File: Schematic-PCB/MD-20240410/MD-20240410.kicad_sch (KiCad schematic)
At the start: 52 parts, among them J1 Conn_01x05_Pin, J2 Conn_01x04_Pin, J3 Conn_01x02_Pin, J4 Conn_01x02_Pin, J5 Conn_01x02_Pin, J6 Conn_01x02_Pin, J7 Conn_01x02_Pin, J8 Conn_01x15_Pin, Q2 PMOS, Q3 NMOS, Q4 NMOS

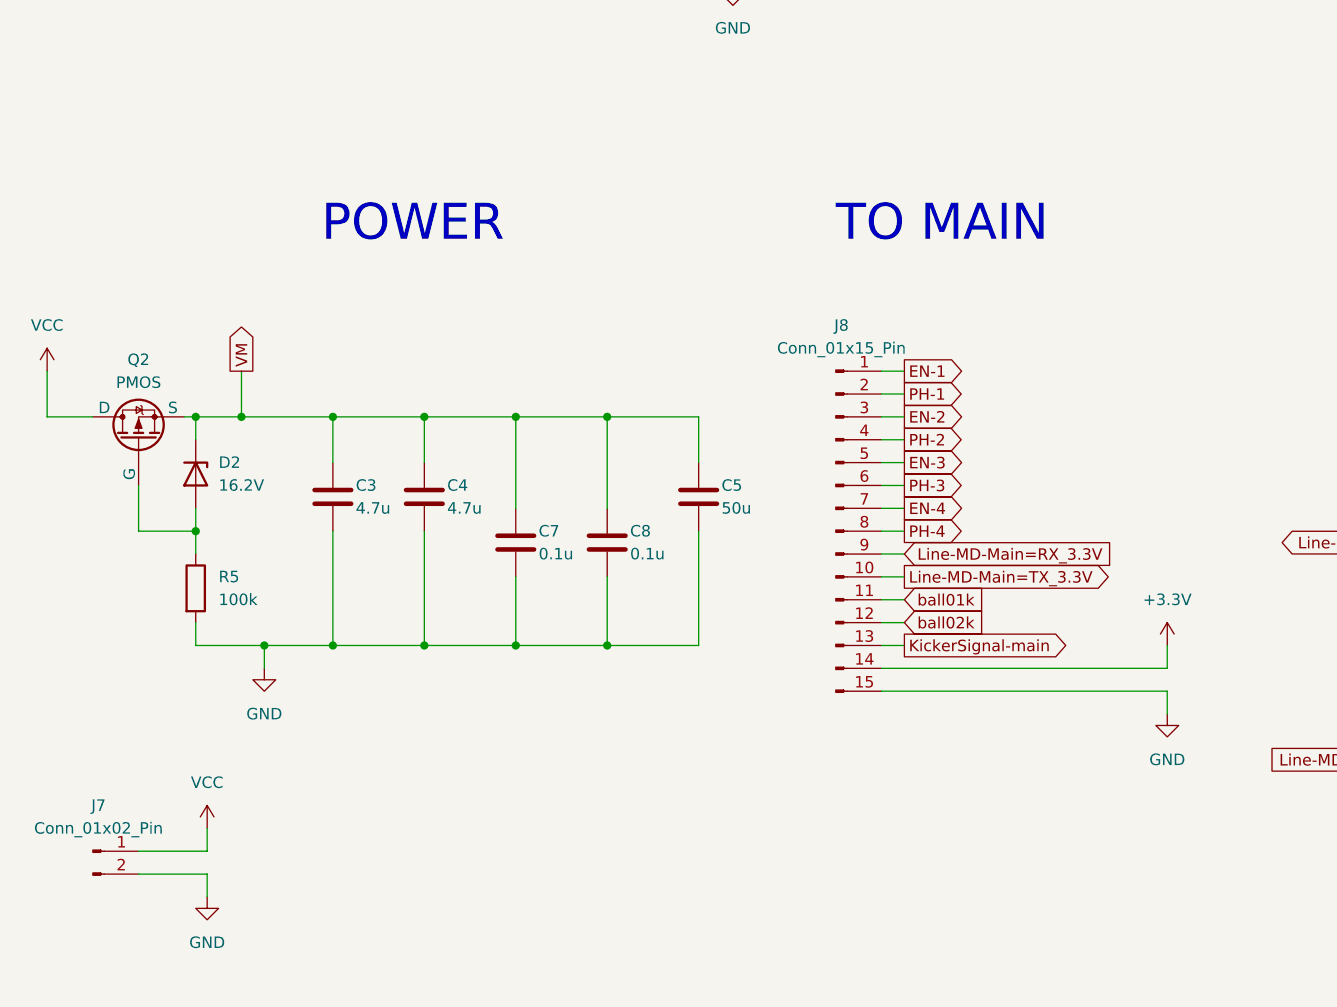
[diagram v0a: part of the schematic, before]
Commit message: MD基板のPCBを更新
回路図のDRを再度お願いしたい
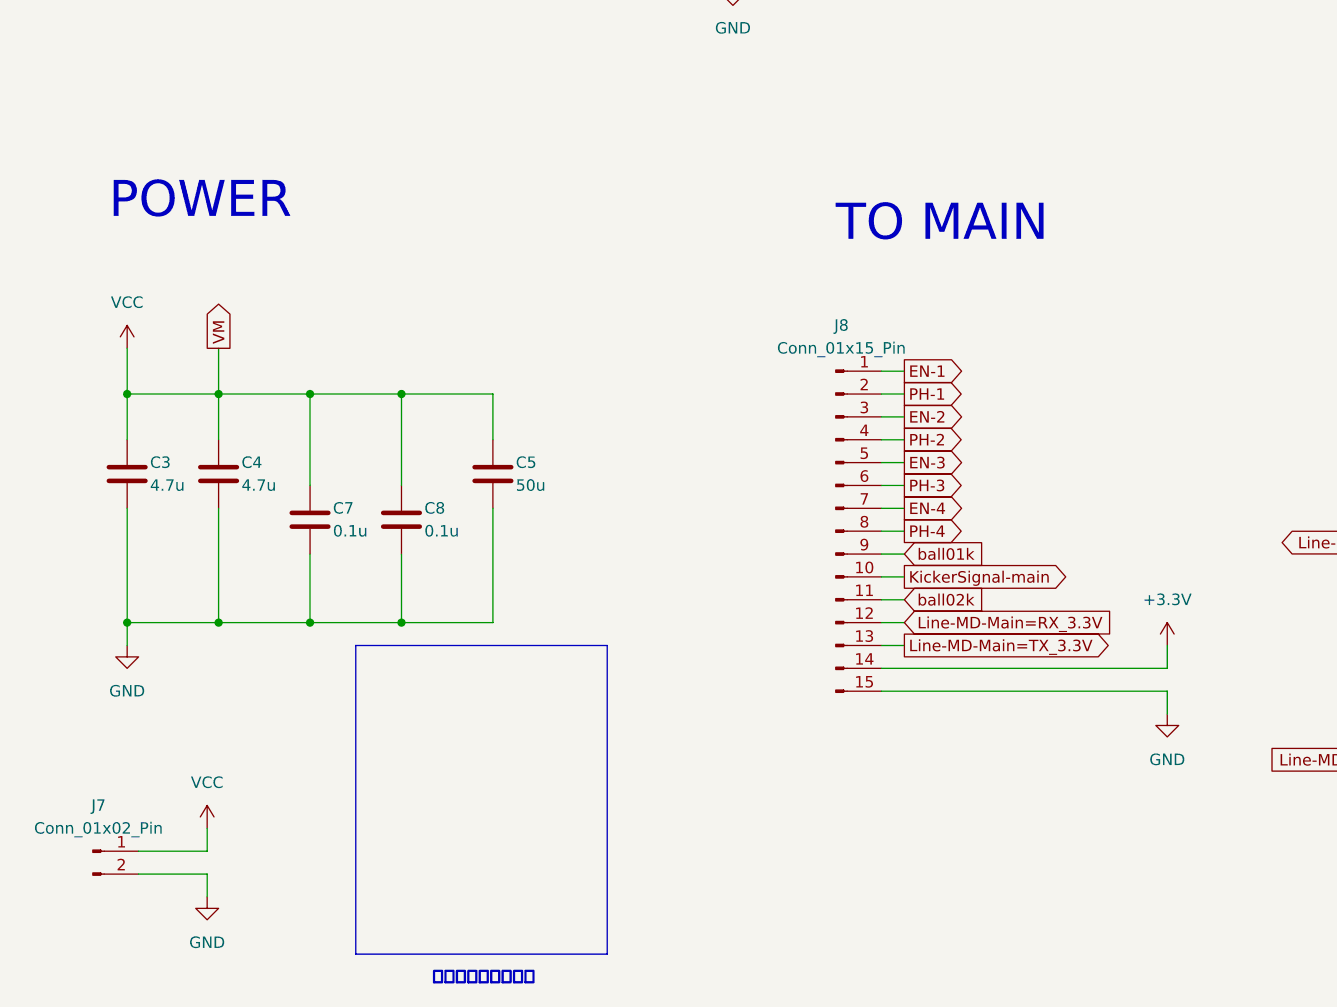
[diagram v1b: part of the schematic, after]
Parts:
- removed D2: 16.2V, Diode_SMD:D_SOD-323, symbol Device:D_Zener
- removed Q2: PMOS, Package_TO_SOT_SMD:TO-252-2, symbol Simulation_SPICE:PMOS
- removed R5: 100k, Resistor_SMD:R_0603_1608Metric, symbol Device:R
- J2: footprint Connector_FFC-FPC:TE_84953-4_1x04-1MP_P1.0mm_Horizontal -> Connector_JST:JST_XH_S4B-XH-A-1_1x04_P2.50mm_Horizontal
- J3, J4, J5, J6: footprint Connector_JST:JST_VH_B2P-VH_1x02_P3.96mm_Vertical -> @2024-MD:JST_VH_B2P-VH-B_1x02_P3.96mm_Vertical
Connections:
- net VM is gone; now on net VCC: C10.2, C12.2, C14.2, C2.2, C3.1, C4.1, C5.1, C7.1, C8.1, U1.11 (VM), U2.11 (VM), U3.11 (VM), U4.11 (VM)
- net KickerSignal-main: now also J8.10 (Pin_10); no longer J8.13 (Pin_13)
- net Line-MD-Main=RX_3.3V: now also J8.12 (Pin_12); no longer J8.9 (Pin_9)
- net Line-MD-Main=TX_3.3V: now also J8.13 (Pin_13); no longer J8.10 (Pin_10)
- net ball01k: now also J8.9 (Pin_9); no longer J8.11 (Pin_11)
- net ball02k: now also J8.11 (Pin_11); no longer J8.12 (Pin_12)
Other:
- note added: "保護部分は削除した"
- moved on the sheet: C3, C4, C5, C7, C8

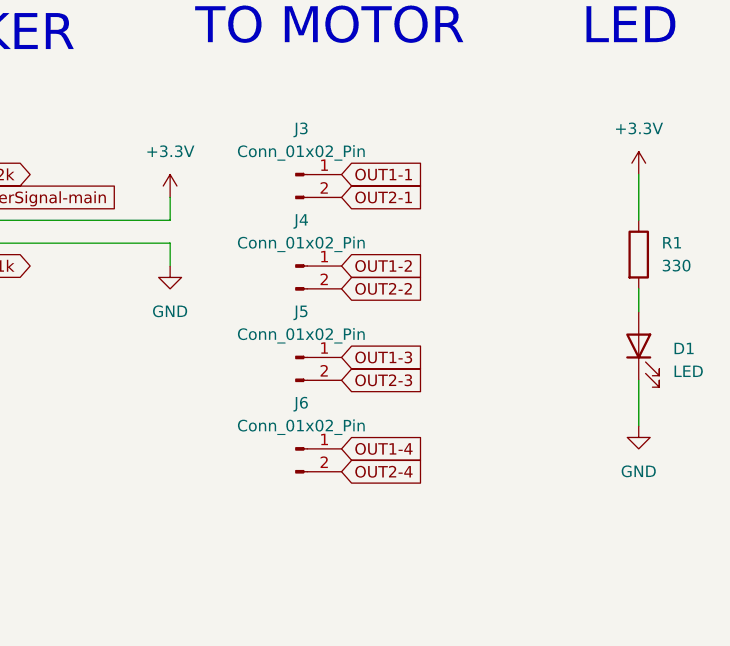
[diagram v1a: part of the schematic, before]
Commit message: MD基板のPCBを更新
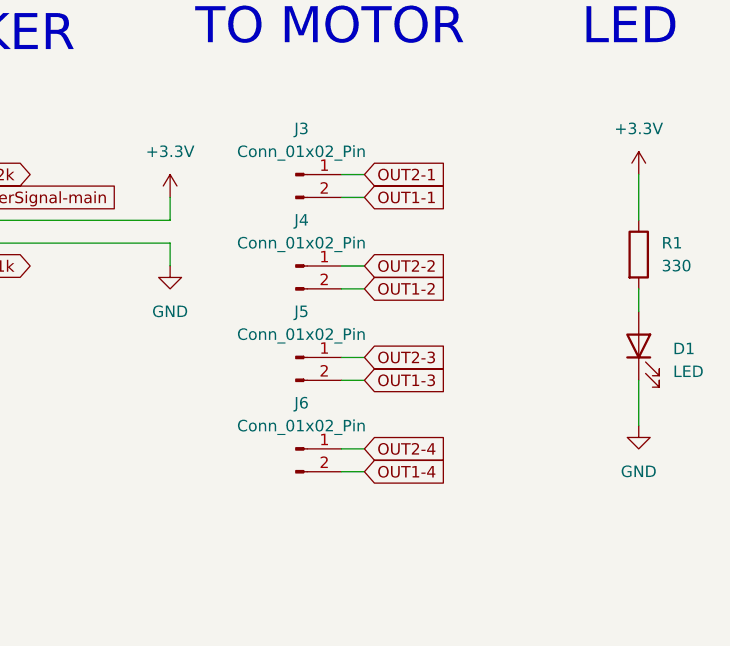
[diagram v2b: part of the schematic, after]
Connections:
- net OUT1-1: now also J3.2 (Pin_2); no longer J3.1 (Pin_1)
- net OUT1-2: now also J4.2 (Pin_2); no longer J4.1 (Pin_1)
- net OUT1-3: now also J5.2 (Pin_2); no longer J5.1 (Pin_1)
- net OUT1-4: now also J6.2 (Pin_2); no longer J6.1 (Pin_1)
- net OUT2-1: now also J3.1 (Pin_1); no longer J3.2 (Pin_2)
- net OUT2-2: now also J4.1 (Pin_1); no longer J4.2 (Pin_2)
- net OUT2-3: now also J5.1 (Pin_1); no longer J5.2 (Pin_2)
- net OUT2-4: now also J6.1 (Pin_1); no longer J6.2 (Pin_2)
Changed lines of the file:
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@@
 	(wire
 		(pts
+			(xy 363.22 215.9) (xy 360.68 215.9)
+		)
+		(stroke
+			(width 0)
+			(type default)
+		)
+	)
+	(wire
+		(pts
 			(xy 234.95 167.64) (xy 234.95 165.1)
 		)
@@
 	(wire
 		(pts
+			(xy 360.68 213.36) (xy 363.22 213.36)
+		)
+		(stroke
+			(width 0)
+			(type default)
+		)
+	)
+	(wire
+		(pts
 			(xy 337.82 146.05) (xy 337.82 148.59)
 		)
@@
 	(wire
 		(pts
+			(xy 360.68 226.06) (xy 363.22 226.06)
+		)
+		(stroke
+			(width 0)
+			(type default)
+		)
+	)
+	(wire
+		(pts
 			(xy 243.84 55.88) (xy 243.84 58.42)
 		)
@@
 	(wire
 		(pts
+			(xy 360.68 236.22) (xy 363.22 236.22)
+		)
+		(stroke
+			(width 0)
+			(type default)
+		)
+	)
+	(wire
+		(pts
+			(xy 360.68 246.38) (xy 363.22 246.38)
+		)
+		(stroke
+			(width 0)
+			(type default)
+		)
+	)
+	(wire
+		(pts
 			(xy 114.3 222.25) (xy 116.84 222.25)
 		)
@@
 	(wire
 		(pts
+			(xy 360.68 233.68) (xy 363.22 233.68)
+		)
+		(stroke
+			(width 0)
+			(type default)
+		)
+	)
+	(wire
+		(pts
 			(xy 284.48 62.23) (xy 299.72 62.23)
 		)
@@
 	(wire
 		(pts
+			(xy 360.68 223.52) (xy 363.22 223.52)
+		)
+		(stroke
+			(width 0)
+			(type default)
+		)
+	)
+	(wire
+		(pts
 			(xy 213.36 231.14) (xy 213.36 233.68)
 		)
@@
 	(wire
 		(pts
+			(xy 360.68 243.84) (xy 363.22 243.84)
+		)
+		(stroke
+			(width 0)
+			(type default)
+		)
+	)
+	(wire
+		(pts
 			(xy 81.28 50.8) (xy 86.36 50.8)
 		)
@@
 	(global_label "OUT1-4"
 		(shape input)
-		(at 360.68 243.84 0)
+		(at 363.22 246.38 0)
 		(fields_autoplaced yes)
 		(effects
@@
 		)
 		(property "Intersheetrefs" "${INTERSHEET_REFS}"
-			(at 371.2852 243.84 0)
+			(at 373.8252 246.38 0)
 			(effects
 				(font
@@
 	(global_label "OUT2-2"
 		(shape input)
-		(at 360.68 226.06 0)
+		(at 363.22 223.52 0)
 		(fields_autoplaced yes)
 		(effects
@@
 		)
 		(property "Intersheetrefs" "${INTERSHEET_REFS}"
-			(at 371.2852 226.06 0)
+			(at 373.8252 223.52 0)
 			(effects
 				(font
@@
 	(global_label "OUT1-1"
 		(shape input)
-		(at 360.68 213.36 0)
+		(at 363.22 215.9 0)
 		(fields_autoplaced yes)
 		(effects
@@
 		)
 		(property "Intersheetrefs" "${INTERSHEET_REFS}"
-			(at 371.2852 213.36 0)
+			(at 373.8252 215.9 0)
 			(effects
 				(font
@@
 	(global_label "OUT1-2"
 		(shape input)
-		(at 360.68 223.52 0)
+		(at 363.22 226.06 0)
 		(fields_autoplaced yes)
 		(effects
@@
 		)
 		(property "Intersheetrefs" "${INTERSHEET_REFS}"
-			(at 371.2852 223.52 0)
+			(at 373.8252 226.06 0)
 			(effects
 				(font
@@
 	(global_label "OUT2-4"
 		(shape input)
-		(at 360.68 246.38 0)
+		(at 363.22 243.84 0)
 		(fields_autoplaced yes)
 		(effects
@@
 		)
 		(property "Intersheetrefs" "${INTERSHEET_REFS}"
-			(at 371.2852 246.38 0)
+			(at 373.8252 243.84 0)
 			(effects
 				(font
@@
 	(global_label "OUT1-3"
 		(shape input)
-		(at 360.68 233.68 0)
+		(at 363.22 236.22 0)
 		(fields_autoplaced yes)
 		(effects
@@
 		)
 		(property "Intersheetrefs" "${INTERSHEET_REFS}"
-			(at 371.2852 233.68 0)
+			(at 373.8252 236.22 0)
 			(effects
 				(font
@@
 	(global_label "OUT2-1"
 		(shape input)
-		(at 360.68 215.9 0)
+		(at 363.22 213.36 0)
 		(fields_autoplaced yes)
 		(effects
@@
 		)
 		(property "Intersheetrefs" "${INTERSHEET_REFS}"
-			(at 371.2852 215.9 0)
+			(at 373.8252 213.36 0)
 			(effects
 				(font
@@
 	(global_label "OUT2-3"
 		(shape input)
-		(at 360.68 236.22 0)
+		(at 363.22 233.68 0)
 		(fields_autoplaced yes)
 		(effects
@@
 		)
 		(property "Intersheetrefs" "${INTERSHEET_REFS}"
-			(at 371.2852 236.22 0)
+			(at 373.8252 233.68 0)
 			(effects
 				(font

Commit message: MDのDRしたよ
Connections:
- net +3.3V: now also J1.4 (Pin_4); no longer J1.3 (Pin_3)
- net +5V: now also J2.1 (Pin_1); no longer J2.3 (Pin_3)
- net GND: now also J1.3 (Pin_3), J2.2 (Pin_2); no longer J1.4 (Pin_4), J2.4 (Pin_4)
- net Line-MD-Main=RX_5V: now also J2.4 (Pin_4); no longer J2.2 (Pin_2)
- net Line-MD-Main=TX_5V: now also J2.3 (Pin_3); no longer J2.1 (Pin_1)
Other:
- moved on the sheet: J1, J3, J4, J5, J6

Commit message: MD基板を修正したよ
XH4ピンの位置を裏側・内側へ直した
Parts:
- J3, J4, J5, J6: footprint @2024-MD:JST_VH_B2P-VH-B_1x02_P3.96mm_Vertical -> @2024TOINIOT2-MD:JST_XH_B2B-XH-A_1x02_P2.50mm_Vertical
- J7: footprint @2024-MD:XT30U-M -> @2024TOINIOT2-MD:XT30U-M
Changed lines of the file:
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@@
 			)
 		)
-		(property "Footprint" "@2024-MD:JST_VH_B2P-VH-B_1x02_P3.96mm_Vertical"
+		(property "Footprint" "@2024TOINIOT2-MD:JST_XH_B2B-XH-A_1x02_P2.50mm_Vertical"
 			(at 360.68 213.36 0)
 			(effects
@@
 			)
 		)
-		(property "Footprint" "@2024-MD:JST_VH_B2P-VH-B_1x02_P3.96mm_Vertical"
+		(property "Footprint" "@2024TOINIOT2-MD:JST_XH_B2B-XH-A_1x02_P2.50mm_Vertical"
 			(at 360.68 233.68 0)
 			(effects
@@
 			)
 		)
-		(property "Footprint" "@2024-MD:JST_VH_B2P-VH-B_1x02_P3.96mm_Vertical"
+		(property "Footprint" "@2024TOINIOT2-MD:JST_XH_B2B-XH-A_1x02_P2.50mm_Vertical"
 			(at 360.68 223.52 0)
 			(effects
@@
 			)
 		)
-		(property "Footprint" "@2024-MD:JST_VH_B2P-VH-B_1x02_P3.96mm_Vertical"
+		(property "Footprint" "@2024TOINIOT2-MD:JST_XH_B2B-XH-A_1x02_P2.50mm_Vertical"
 			(at 360.68 243.84 0)
 			(effects
@@
 			)
 		)
-		(property "Footprint" "@2024-MD:XT30U-M"
+		(property "Footprint" "@2024TOINIOT2-MD:XT30U-M"
 			(at 26.67 267.97 0)
 			(effects

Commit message: MD基板とキッカー基板を編集した
接続方法をピンヘッダ&ピンソケットに変更してみた
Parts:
- removed D1: LED, LED_SMD:LED_0805_2012Metric, symbol Device:LED
- removed R1: 330, Resistor_SMD:R_0603_1608Metric, symbol Device:R
- removed U1, U2, U3, U4: ~, Package_SO:HTSSOP-16-1EP_4.4x5mm_P0.65mm_EP3.4x5mm_Mask2.46x2.31mm, symbol @MyLibrary:DRV8874
- added D1: PWR, LED_SMD:LED_0805_2012Metric, symbol Device:LED_Small_Filled
- added R1: 330, Resistor_SMD:R_0603_1608Metric, symbol Device:R_Small
- added U1, U2, U3, U4: ~, Package_SO:HTSSOP-16-1EP_4.4x5mm_P0.65mm_EP3.4x5mm, symbol @2024TOINIOT2-MD:DRV8874
- J1: footprint Connector_JST:JST_XH_S5B-XH-A-1_1x05_P2.50mm_Horizontal -> Connector_PinSocket_2.54mm:PinSocket_1x05_P2.54mm_Horizontal
- R10, R14, R18, R6: now not fitted
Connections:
- net +3.3V: now also R1.1, U1.3 (SLEEP), U2.3 (SLEEP), U3.3 (SLEEP), U4.3 (SLEEP)
- net EN-1: now also U1.1 (EN)
- net EN-2: now also U2.1 (EN)
- net EN-3: now also U3.1 (EN)
- net EN-4: now also U4.1 (EN)
- net GND: now also D1.1 (K), U1.15 (GND), U1.16 (PMODE), U1.17 (GND), U1.9 (PGND), U2.15 (GND), U2.16 (PMODE), U2.17 (GND), U2.9 (PGND), U3.15 (GND), U3.16 (PMODE), U3.17 (GND), U3.9 (PGND), U4.15 (GND), U4.16 (PMODE), U4.17 (GND), U4.9 (PGND)
- net IMODE-1: now also U1.7 (IMODE)
- net IMODE-2: now also U2.7 (IMODE)
- net IMODE-3: now also U3.7 (IMODE)
- net IMODE-4: now also U4.7 (IMODE)
- net OUT1-1: now also U1.8 (OUT1)
- net OUT1-2: now also U2.8 (OUT1)
- net OUT1-3: now also U3.8 (OUT1)
- net OUT1-4: now also U4.8 (OUT1)
- net OUT2-1: now also U1.10 (OUT2)
- net OUT2-2: now also U2.10 (OUT2)
- net OUT2-3: now also U3.10 (OUT2)
- net OUT2-4: now also U4.10 (OUT2)
- net PH-1: now also U1.2 (PH)
- net PH-2: now also U2.2 (PH)
- net PH-3: now also U3.2 (PH)
- net PH-4: now also U4.2 (PH)
- net VCC: now also U1.11 (VM), U2.11 (VM), U3.11 (VM), U4.11 (VM)
- net VREF-1: now also U1.5 (VREF)
- net VREF-2: now also U2.5 (VREF)
- net VREF-3: now also U3.5 (VREF)
- net VREF-4: now also U4.5 (VREF)
- net at R4.1: now also U1.6 (IPROPI)
- net at R16.1: now also U4.6 (IPROPI)
- net at C10.1: now also U2.12 (VCP)
- net at C9.2: now also U2.13 (CPH)
- net at C9.1: now also U2.14 (CPL)
- net at R8.1: now also U2.6 (IPROPI)
- net at C12.1: now also U3.12 (VCP)
- net at C14.1: now also U4.12 (VCP)
- net at C11.1: now also U3.14 (CPL)
- net at C11.2: now also U3.13 (CPH)
- net at C13.2: now also U4.13 (CPH)
- net at C13.1: now also U4.14 (CPL)
- net at C2.1: now also U1.12 (VCP)
- net at R12.1: now also U3.6 (IPROPI)
- net at C1.1: now also U1.14 (CPL)
- net at C1.2: now also U1.13 (CPH)
- new net: D1.2 (A), R1.2
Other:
- note added: "LEVEL CONVERT"
- note removed: "LED"
- note removed: "LEVEL"
- note removed: "保護部分は削除した"
- moved on the sheet: C1, C10, C11, C12, C13, C14, C2, C3, C4, C5, C7, C8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
